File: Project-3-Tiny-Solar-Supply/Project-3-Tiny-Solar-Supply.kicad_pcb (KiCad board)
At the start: 2 copper layers, 16 parts, among them J1 Conn_01x02_Pin, J2 Conn_01x02_Pin, J3 Conn_01x02_Pin, J4 Conn_01x02_Pin, Q1 2N7002, U1 AP3015AKTR-G1

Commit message: arrange footprints
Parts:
- moved D2 234.3 mm to (49.5, 84.8)
- moved Q1 227.9 mm to (49.0, 99.8)
- moved J3 225.7 mm to (48.5, 90.2), turned to 90 degrees
- moved J2 224.8 mm to (43.0, 97.8)
- moved D1 224.4 mm to (58.8, 85.0)
- moved J4 223.8 mm to (42.6, 92.8), turned to 180 degrees
- moved U1 216.1 mm to (58.0, 90.2)
- moved C2 211.4 mm to (61.0, 100.5)
- moved C1 208.5 mm to (68.8, 97.3)
- moved C3 208.5 mm to (68.8, 100.5)
- moved R3 204.6 mm to (54.0, 97.3)
- moved R4 204.5 mm to (54.0, 100.8)
- moved L1 199.9 mm to (67.5, 88.5), turned to -90 degrees
- moved R2 199.3 mm to (58.8, 97.3)
- moved R1 194.0 mm to (63.5, 97.3)
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
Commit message: update associated footprints for J1, J2, J3
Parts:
- J1, J2: footprint Connector_PinHeader_2.54mm:PinHeader_1x02_P2.54mm_Vertical -> Connector_PinHeader_2.54mm:PinHeader_1x02_P2.54mm_Horizontal
- moved J4 2.50 mm to (42.6, 90.2)
- moved J1 0.75 mm to (74.8, 94.2)
- moved J2 0.25 mm to (42.8, 97.8), turned to 180 degrees

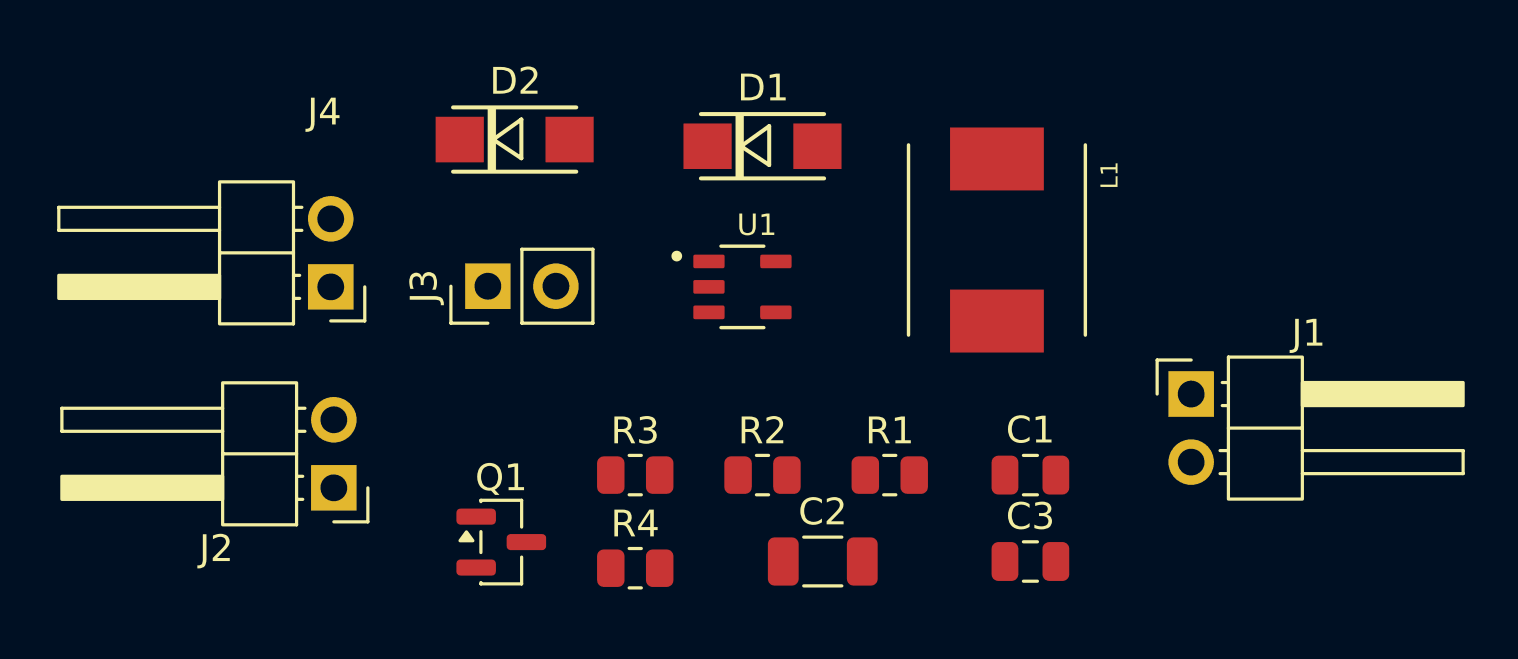
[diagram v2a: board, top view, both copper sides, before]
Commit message: update associated footprint for J3 (from jumper connector to button switch)
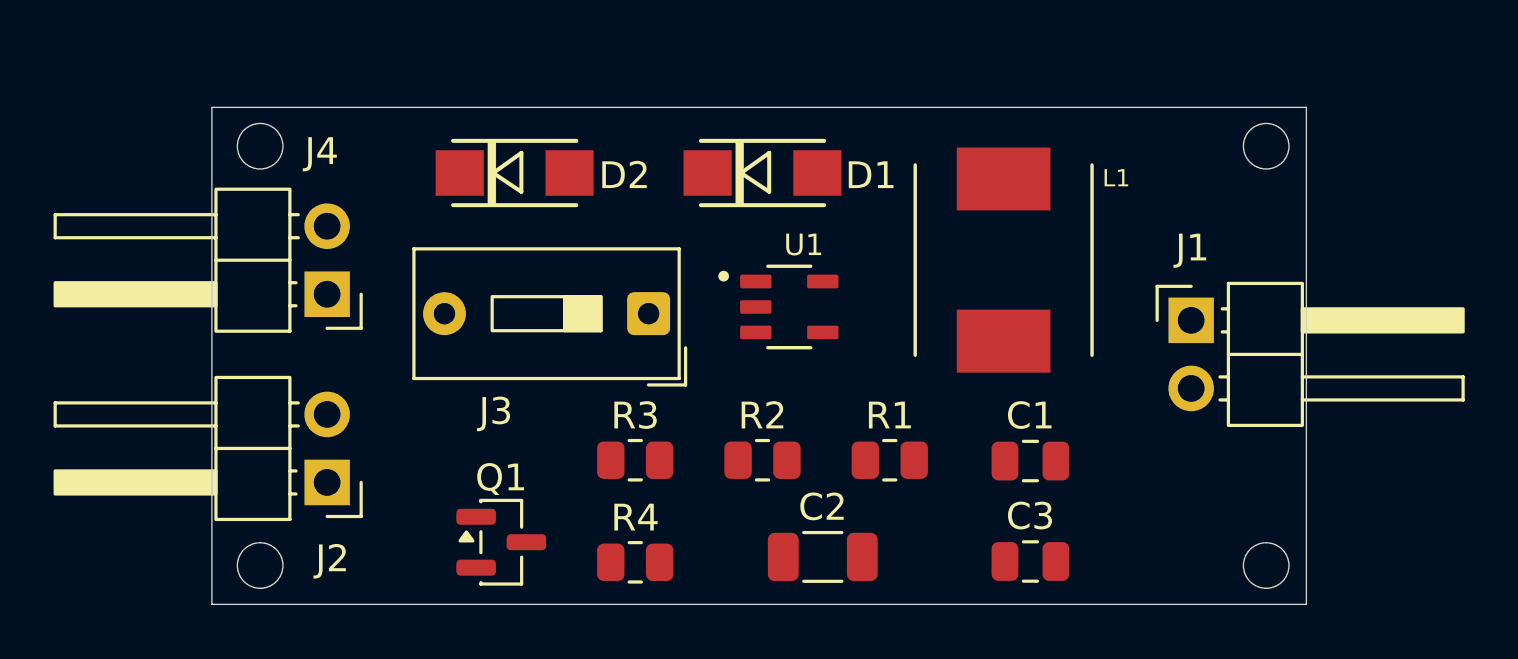
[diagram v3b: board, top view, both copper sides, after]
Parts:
- J3: footprint Connector_PinHeader_2.54mm:PinHeader_1x02_P2.54mm_Vertical -> Button_Switch_THT:SW_DIP_SPSTx01_Slide_9.78x4.72mm_W7.62mm_P2.54mm
- moved J3 6.09 mm to (54.5, 91.2), turned to 180 degrees
- moved J1 2.75 mm to (74.8, 91.5)
- moved U1 1.90 mm to (59.8, 91.0)
- moved D2 1.25 mm to (49.5, 86.0)
- moved D1 1.00 mm to (58.8, 86.0)
- moved L1 0.79 mm to (67.8, 89.2)
- moved R1 0.56 mm to (63.5, 96.7)
- moved R2 0.56 mm to (58.8, 96.7)
- moved R3 0.56 mm to (54.0, 96.7)
- moved C1 0.53 mm to (68.8, 96.8)
- moved J2 0.32 mm to (42.5, 97.5)
- moved J4 0.31 mm to (42.5, 90.5)
- moved R4 0.22 mm to (54.0, 100.5)
- moved C2 0.17 mm to (61.0, 100.3)
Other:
- board outline added: 40.8 x 18.5 mm
